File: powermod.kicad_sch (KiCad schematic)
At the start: 16 parts, among them J1 Conn_02x07_Odd_Even, J2 Conn_02x07_Odd_Even, U1 TPS54202

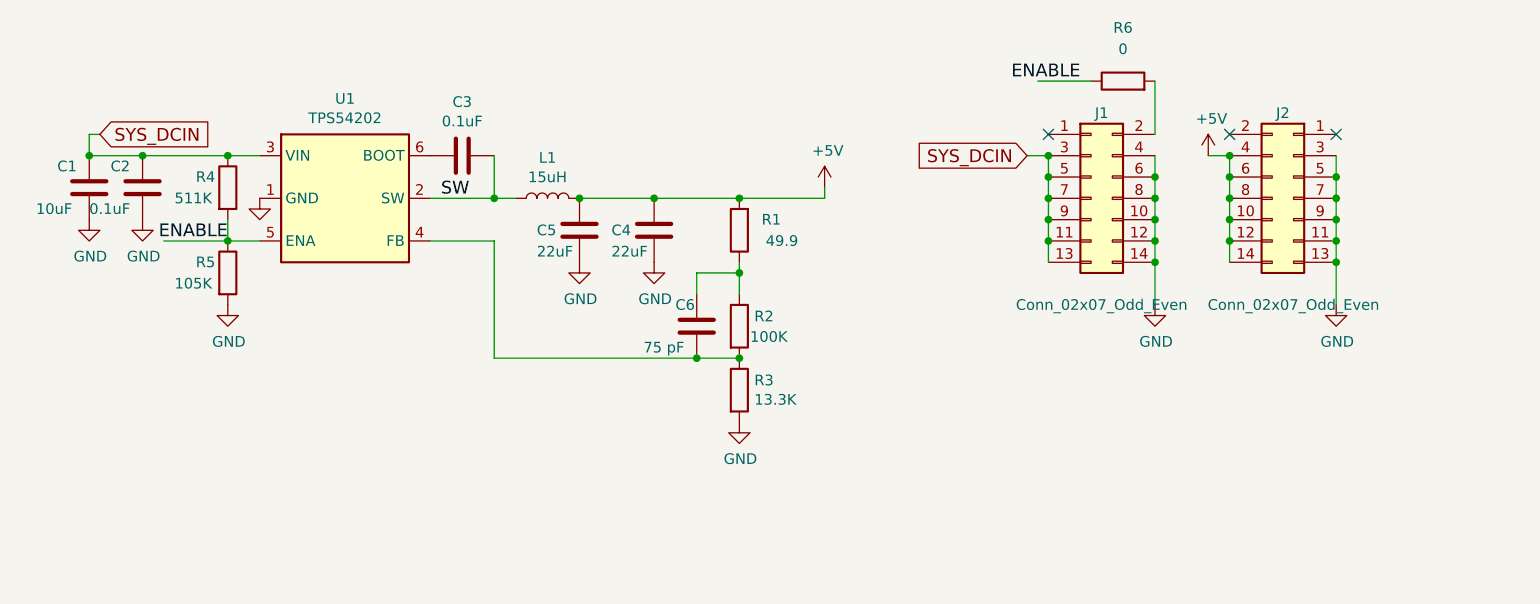
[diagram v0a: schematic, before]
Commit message: powermod-tps54260
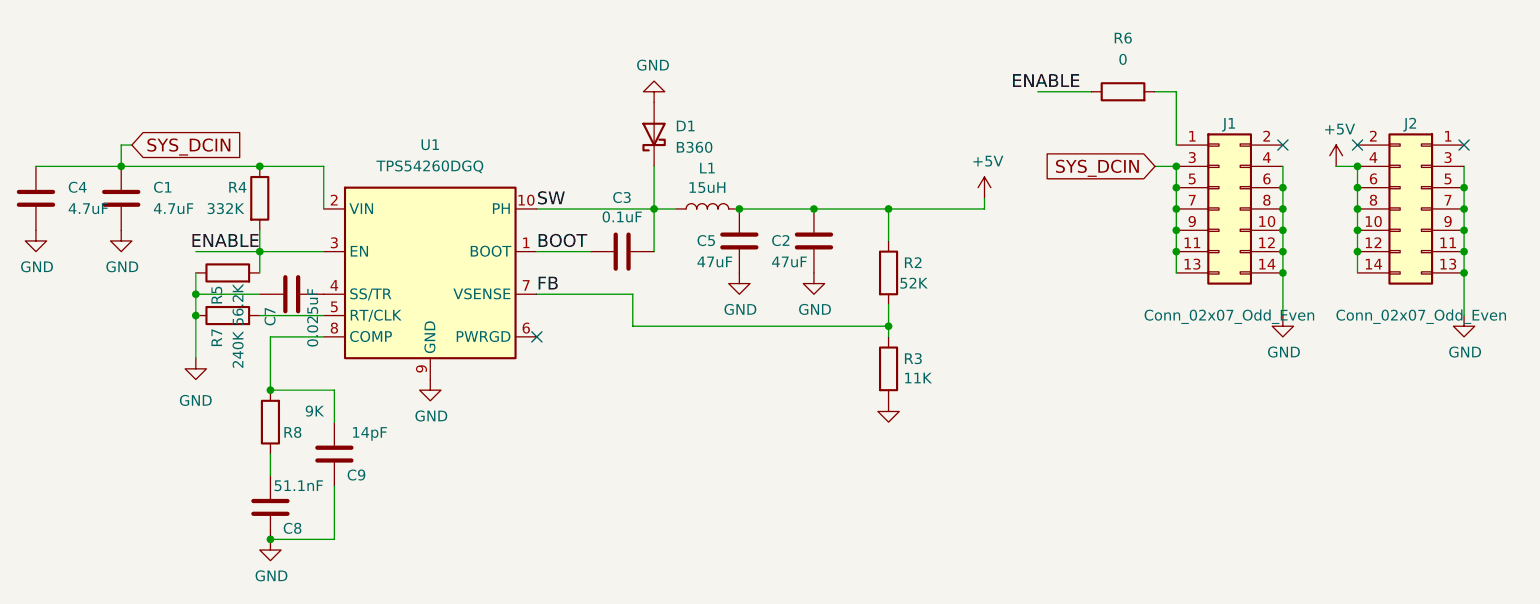
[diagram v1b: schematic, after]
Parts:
- removed C6: 75 pF, Capacitor_SMD:C_0402_1005Metric, symbol Device:C
- removed R1: 49.9, Resistor_SMD:R_0402_1005Metric, symbol Device:R
- removed U1: TPS54202, Package_TO_SOT_SMD:SOT-23-6, symbol tps54202:TPS54202
- added C7: 0.025uF, Capacitor_SMD:C_0402_1005Metric, symbol Device:C
- added C8: 51.1nF, Capacitor_SMD:C_0402_1005Metric, symbol Device:C
- added C9: 14pF, Capacitor_SMD:C_0402_1005Metric, symbol Device:C
- added D1: B360, Diode_SMD:D_SMC, symbol Diode:B360
- added R7: 240K, Resistor_SMD:R_0402_1005Metric, symbol Device:R
- added R8: 9K, Resistor_SMD:R_0402_1005Metric, symbol Device:R
- added U1: TPS54260DGQ, Package_SO:MSOP-10-1EP_3x3mm_P0.5mm_EP2.2x3.1mm_Mask1.83x1.89mm_ThermalVias, symbol Regulator_Switching:TPS54260DGQ
- C1: value 10uF -> 4.7uF; footprint Capacitor_SMD:C_0603_1608Metric -> Capacitor_SMD:C_1210_3225Metric
- C2: value 0.1uF -> 47uF; footprint Capacitor_SMD:C_0402_1005Metric -> Capacitor_SMD:C_0805_2012Metric
- C4: value 22uF -> 4.7uF; footprint Capacitor_SMD:C_0805_2012Metric -> Capacitor_SMD:C_1210_3225Metric
- C5: value 22uF -> 47uF
- R2: value 100K -> 52K
- R3: value 13.3K -> 11K
- R4: value 511K -> 332K
- R5: value 105K -> 56.2K
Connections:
- net +5V: now also C2.1, R2.1; no longer C4.1
- net ENABLE: now also R5.2, U1.3 (EN); no longer R5.1
- net GND: now also R5.1, C7.1, C8.1, C9.1, D1.2 (A), R7.1, U1.9 (GND); no longer R5.2
- net SW: now also D1.1 (K), U1.10 (PH)
- net SYS_DCIN: now also C4.1, U1.2 (VIN); no longer C2.1
- net FB: now reaches R2.2, R3.1
- net FB: now also U1.7 (VSENSE)
- net BOOT: now reaches C3.2
- net BOOT: now also U1.1 (BOOT)
- net at J1.1 (Pin_1): now also R6.2
- net at J1.2 (Pin_2): no longer R6.2
- new net: C8.2, R8.1
- new net: C9.2, R8.2, U1.8 (COMP)
- new net: C7.2, U1.4 (SS/TR)
- new net: R7.2, U1.5 (RT/CLK)
- no-connect marks 3 -> 4
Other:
- title: powermod-tps54202-3.0 -> powermod-tps54260-1.2
- moved on the sheet: C3, C5, J1, J2, L1, R2, R3, R4, R5, R6
